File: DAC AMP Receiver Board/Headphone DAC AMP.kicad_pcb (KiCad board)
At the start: 4 copper layers, 55.2 x 67.7 mm, 75 parts, among them J3 SJ-3502-SMT, U1 ES9039Q2M, U2 TPS7A39, U3 TPA6120A2DWP, U4 OPA1612AxD, U5 OPA1612AxD, U6 TPS7A20xxxDQN

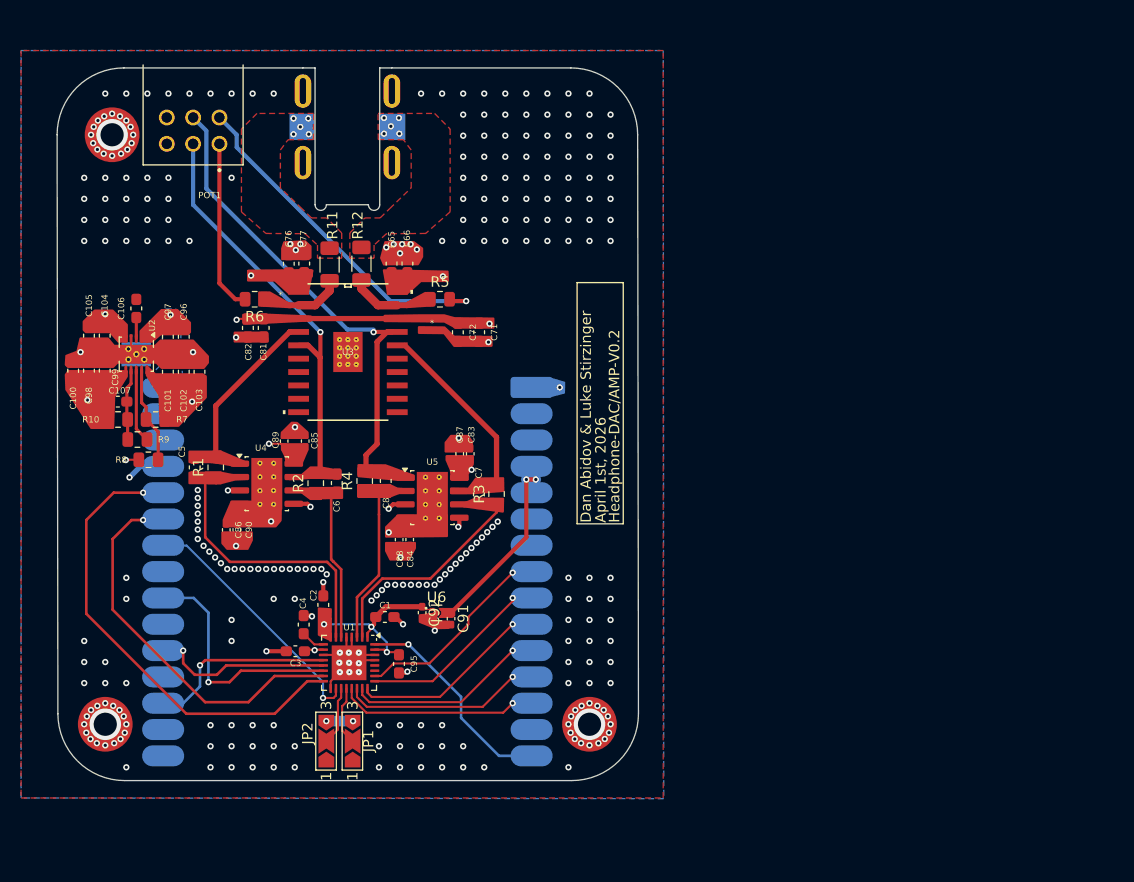
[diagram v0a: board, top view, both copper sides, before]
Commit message: Boards in same project, not panelized yet
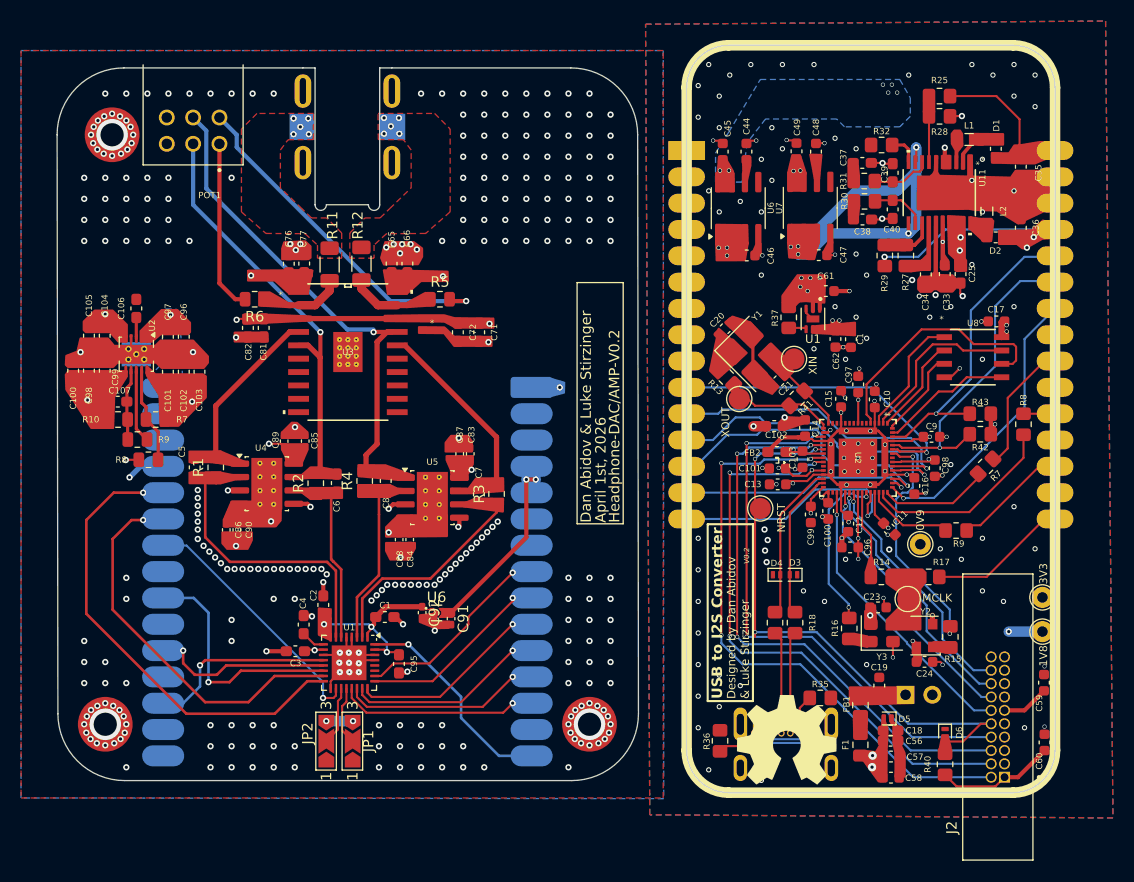
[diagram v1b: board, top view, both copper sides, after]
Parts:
- added 0V9: TestPoint_Probe, TestPoint:TestPoint_THTPad_D2.0mm_Drill1.0mm, F.Cu at (164.0, 98.3)
- added 1V8: TestPoint_Probe, TestPoint:TestPoint_THTPad_D2.0mm_Drill1.0mm, F.Cu at (175.6, 106.6)
- added 3V3: TestPoint_Probe, TestPoint:TestPoint_THTPad_D2.0mm_Drill1.0mm, F.Cu at (175.6, 103.3)
- added B**: Castellated Pins, Library:Castellated Hole PCB, F.Cu at (159.3, 60.9)
- added C1: 10u, Capacitor_SMD:C_0603_1608Metric, F.Cu at (157.4, 78.8)
- added C10: 100n, Capacitor_SMD:C_0603_1608Metric, F.Cu at (159.6, 84.5)
- added C100: 100n, Capacitor_SMD:C_0603_1608Metric, F.Cu at (155.2, 95.1)
- added C101: 100n, Capacitor_SMD:C_0603_1608Metric, F.Cu at (150.4, 91.1)
- added C102: 100n, Capacitor_SMD:C_0603_1608Metric, F.Cu at (150.1, 87.1)
- added C103: 1u, Capacitor_SMD:C_0603_1608Metric, F.Cu at (152.8, 90.2)
- added C11: 100n, Capacitor_SMD:C_0603_1608Metric, F.Cu at (161.0, 96.9)
- added C12: 100n, Capacitor_SMD:C_0603_1608Metric, F.Cu at (157.1, 96.3)
- added C13: 100n, Capacitor_SMD:C_0603_1608Metric, F.Cu at (150.4, 92.6)
- added C14: 100n, Capacitor_SMD:C_0603_1608Metric, F.Cu at (153.0, 87.3)
- added C15: 100n, Capacitor_SMD:C_0603_1608Metric, F.Cu at (156.4, 84.5)
- added C16: 100n, Capacitor_SMD:C_0603_1608Metric, F.Cu at (163.4, 92.8)
- added C17: 100n, Capacitor_SMD:C_0603_1608Metric, F.Cu at (171.2, 77.1)
- added C18: 100n, Capacitor_SMD:C_0603_1608Metric, F.Cu at (161.1, 116.0)
- added C19: 100n, Capacitor_SMD:C_0603_1608Metric, F.Cu at (160.1, 111.7)
- added C20: 18p, Capacitor_SMD:C_0603_1608Metric, F.Cu at (145.4, 77.8)
- added C21: 18p, Capacitor_SMD:C_0603_1608Metric, F.Cu at (150.5, 82.8)
- added C23: 100n, Capacitor_SMD:C_0603_1608Metric, F.Cu at (160.0, 104.3)
- added C24: 100n, Capacitor_SMD:C_0603_1608Metric, F.Cu at (164.4, 109.5)
- added C25: 10u, Capacitor_SMD:C_0603_1608Metric_Pad1.08x0.95mm_HandSolder, F.Cu at (167.8, 72.6)
- added C33: 1u, Capacitor_SMD:C_0603_1608Metric_Pad1.08x0.95mm_HandSolder, F.Cu at (166.3, 72.6)
- added C34: 1u, Capacitor_SMD:C_0603_1608Metric_Pad1.08x0.95mm_HandSolder, F.Cu at (164.5, 72.7)
- added C35: 10u, Capacitor_SMD:C_0603_1608Metric_Pad1.08x0.95mm_HandSolder, F.Cu at (173.5, 62.4)
- added C36: 10u, Capacitor_SMD:C_0603_1608Metric_Pad1.08x0.95mm_HandSolder, F.Cu at (173.5, 68.2)
- added C37: 330p, Capacitor_SMD:C_0603_1608Metric_Pad1.08x0.95mm_HandSolder, F.Cu at (158.5, 62.1)
- added C38: 18n, Capacitor_SMD:C_0603_1608Metric_Pad1.08x0.95mm_HandSolder, F.Cu at (158.5, 67.5)
- added C39: 22p, Capacitor_SMD:C_0603_1608Metric_Pad1.08x0.95mm_HandSolder, F.Cu at (161.3, 63.0)
- added C40: 39p, Capacitor_SMD:C_0603_1608Metric_Pad1.08x0.95mm_HandSolder, F.Cu at (161.3, 66.5)
- added C44: 1u, Capacitor_SMD:C_0603_1608Metric, F.Cu at (147.5, 61.0)
- added C45: 1u, Capacitor_SMD:C_0603_1608Metric, F.Cu at (145.2, 61.0)
- added C46: 10u, Capacitor_SMD:C_0603_1608Metric, F.Cu at (147.5, 70.9)
- added C47: 10u, Capacitor_SMD:C_0603_1608Metric, F.Cu at (154.3, 70.8)
- added C48: 1u, Capacitor_SMD:C_0603_1608Metric, F.Cu at (154.1, 61.0)
- added C49: 1u, Capacitor_SMD:C_0603_1608Metric, F.Cu at (152.2, 61.0)
- added C56: 100n, Capacitor_SMD:C_0603_1608Metric, F.Cu at (161.1, 117.0)
- added C57: 1u, Capacitor_SMD:C_0603_1608Metric, F.Cu at (161.2, 118.5)
- added C58: 1u, Capacitor_SMD:C_0603_1608Metric, F.Cu at (161.2, 120.5)
- added C59: 100n, Capacitor_SMD:C_0603_1608Metric, F.Cu at (175.7, 111.4)
- added C60: 100n, Capacitor_SMD:C_0603_1608Metric, F.Cu at (175.8, 117.1)
- added C61: 1u, Capacitor_SMD:C_0603_1608Metric, F.Cu at (155.0, 74.2)
- added C62: 10u, Capacitor_SMD:C_0603_1608Metric, F.Cu at (155.9, 78.8)
- added C9: 100n, Capacitor_SMD:C_0603_1608Metric, F.Cu at (165.0, 88.1)
- added C96: 100n, Capacitor_SMD:C_0603_1608Metric, F.Cu at (157.3, 98.6)
- added C97: 100n, Capacitor_SMD:C_0603_1608Metric, F.Cu at (158.1, 83.1)
- added C98: 100n, Capacitor_SMD:C_0603_1608Metric, F.Cu at (165.3, 91.1)
- added C99: 100n, Capacitor_SMD:C_0603_1608Metric, F.Cu at (153.6, 95.5)
- added D1: D_Schottky, Capacitor_SMD:C_0603_1608Metric_Pad1.08x0.95mm_HandSolder, F.Cu at (171.1, 60.7)
- added D2: D_Schottky, Capacitor_SMD:C_0603_1608Metric_Pad1.08x0.95mm_HandSolder, F.Cu at (171.1, 69.1)
- added D3: PESD5V0L1BSL, Diode_SMD:D_SOD-882, F.Cu at (151.9, 101.2)
- added D4: PESD5V0L1BSL, Diode_SMD:D_SOD-882, F.Cu at (150.3, 101.2)
- added D5: PESD5V0L1BSL, Diode_SMD:D_SOD-882, F.Cu at (160.9, 114.8)
- added D6: PESD5V0L1BSL, Diode_SMD:D_SOD-882, F.Cu at (166.3, 116.2)
- added F1: 2A, Fuse:Fuse_0805_2012Metric_Pad1.15x1.40mm_HandSolder, F.Cu at (158.3, 117.3)
- added FB1: 220R, Capacitor_SMD:C_0805_2012Metric_Pad1.18x1.45mm_HandSolder, F.Cu at (158.3, 113.6)
- added FB2: 600R @ 100MHz, Capacitor_SMD:C_0603_1608Metric_Pad1.08x0.95mm_HandSolder, F.Cu at (150.4, 89.5)
- added G***: LOGO, LOGO, F.Cu at (151.3, 116.9)
- added G***: LOGO, LOGO, B.Cu at (168.8, 120.9)
- added G***: LOGO, LOGO, B.Cu at (168.8, 80.9)
- added G***: LOGO, LOGO, B.Cu at (148.8, 120.9)
- added G***: LOGO, LOGO, B.Cu at (148.8, 100.9)
- added G***: LOGO, LOGO, B.Cu at (168.8, 100.9)
- added G***: LOGO, LOGO, B.Cu at (148.8, 80.9)
- added G***: LOGO, LOGO, B.Cu at (148.8, 60.9)
- added G***: LOGO, LOGO, B.Cu at (168.8, 60.9)
- added J1: 2137160001, 2137160001:MOLEX_2137160001, B.Cu at (151.2, 122.5)
- added J2: M50-3551042, M50_3551042:HARWIN_M50-3551042, F.Cu at (171.3, 114.7)
- added J4: PINHD_1x2_Male, Connector_PinHeader_2.54mm:PinHeader_1x02_P2.54mm_Vertical, B.Cu at (162.6, 112.6)
- added L1: 0.82u, Inductor_SMD:L_0805_2012Metric, F.Cu at (168.6, 59.9)
- added L2: 10u, Inductor_SMD:L_0805_2012Metric, F.Cu at (170.3, 66.7)
- added MCLK: TestPoint_Probe, TestPoint:TestPoint_Pad_D2.0mm, F.Cu at (162.8, 103.5)
- added NRST: TestPoint_Probe, TestPoint:TestPoint_Pad_D2.0mm, F.Cu at (148.8, 94.9)
- added R13: 220, Resistor_SMD:R_0805_2012Metric_Pad1.20x1.40mm_HandSolder, F.Cu at (145.5, 82.4)
- added R14: 22, Resistor_SMD:R_0805_2012Metric_Pad1.20x1.40mm_HandSolder, F.Cu at (160.3, 101.4)
- added R15: 22, Resistor_SMD:R_0805_2012Metric_Pad1.20x1.40mm_HandSolder, F.Cu at (166.8, 107.1)
- added R16: 22, Resistor_SMD:R_0805_2012Metric_Pad1.20x1.40mm_HandSolder, F.Cu at (157.2, 106.3)
- added R17: 22, Resistor_SMD:R_0805_2012Metric_Pad1.20x1.40mm_HandSolder, F.Cu at (164.8, 101.4)
- added R18: 22, Resistor_SMD:R_0805_2012Metric_Pad1.20x1.40mm_HandSolder, F.Cu at (152.1, 105.7)
- added R19: 22, Resistor_SMD:R_0805_2012Metric_Pad1.20x1.40mm_HandSolder, F.Cu at (150.2, 105.7)
- added R25: 13K, Resistor_SMD:R_0805_2012Metric_Pad1.20x1.40mm_HandSolder, F.Cu at (165.8, 57.6)
- added R27: 10.7k, Resistor_SMD:R_0805_2012Metric_Pad1.20x1.40mm_HandSolder, F.Cu at (162.6, 70.9)
- added R28: 84.5K, Resistor_SMD:R_0805_2012Metric_Pad1.20x1.40mm_HandSolder, F.Cu at (165.8, 55.7)
- added R29: 90.9k, Resistor_SMD:R_0805_2012Metric_Pad1.20x1.40mm_HandSolder, F.Cu at (160.6, 70.9)
- added R30: 9.09k, Resistor_SMD:R_0805_2012Metric_Pad1.20x1.40mm_HandSolder, F.Cu at (158.7, 65.7)
- added R31: 15k, Resistor_SMD:R_0805_2012Metric_Pad1.20x1.40mm_HandSolder, F.Cu at (158.6, 63.8)
- added R32: DNP, Resistor_SMD:R_0805_2012Metric_Pad1.20x1.40mm_HandSolder, F.Cu at (160.3, 60.4)
- added R35: 5.1k, Resistor_SMD:R_0805_2012Metric_Pad1.20x1.40mm_HandSolder, F.Cu at (154.5, 112.9)
- added R36: 5.1k, Resistor_SMD:R_0805_2012Metric_Pad1.20x1.40mm_HandSolder, F.Cu at (144.9, 117.0)
- added R37: 100k, Resistor_SMD:R_0805_2012Metric_Pad1.20x1.40mm_HandSolder, F.Cu at (151.5, 76.7)
- added R40: 10K, Resistor_SMD:R_0805_2012Metric_Pad1.20x1.40mm_HandSolder, F.Cu at (166.3, 119.2)
- added R41: 1M, Resistor_SMD:R_0805_2012Metric_Pad1.20x1.40mm_HandSolder, F.Cu at (152.3, 84.4)
- added R42: 2k, Resistor_SMD:R_0805_2012Metric_Pad1.20x1.40mm_HandSolder, F.Cu at (169.7, 87.8)
- added R43: 2k, Resistor_SMD:R_0805_2012Metric_Pad1.20x1.40mm_HandSolder, F.Cu at (169.7, 85.9)
- added R7: 10, Resistor_SMD:R_0805_2012Metric_Pad1.20x1.40mm_HandSolder, F.Cu at (170.2, 90.9)
- added R8: 10, Resistor_SMD:R_0805_2012Metric_Pad1.20x1.40mm_HandSolder, F.Cu at (173.8, 86.9)
- added R9: 10, Resistor_SMD:R_0805_2012Metric_Pad1.20x1.40mm_HandSolder, F.Cu at (167.4, 97.0)
- added U1: NCV8187AMTW090TAG, NCV8187AMTW090TAG:SON65P200X200X80-7N, F.Cu at (153.8, 76.9)
- added U11: ADP5071AREZ-R7, ADP5071:RE-20-1_ADI, F.Cu at (165.8, 64.9)
- added U2: XU316-1024-QF60B-C24, footprints:QFN_F60B-C24_XMO, F.Cu at (158.0, 90.1)
- added U6: MCP1727-1802xSN, Package_SO:SOIC-8_3.9x4.9mm_P1.27mm, F.Cu at (146.7, 66.4)
- added U7: MCP1727-3302xSN, Package_SO:SOIC-8_3.9x4.9mm_P1.27mm, F.Cu at (153.5, 66.3)
- added U8: W25Q16JVSNIQ, W25Q16JVSNIQ:SOIC_150MIL_WIN, F.Cu at (169.0, 80.5)
- added XIN: TestPoint_Probe, TestPoint:TestPoint_Pad_D2.0mm, F.Cu at (152.0, 80.7)
- added XOUT: TestPoint_Probe, TestPoint:TestPoint_Pad_D2.0mm, F.Cu at (146.8, 84.5)
- added Y1: Crystal_GND24, Crystal:Crystal_SMD_3225-4Pin_3.2x2.5mm_HandSoldering, F.Cu at (148.0, 80.2)
- added Y2: LMK6CE049152CDLFR, Oscillator:Oscillator_SMD_EuroQuartz_XO32-4Pin_3.2x2.5mm, F.Cu at (164.4, 107.0)
- added Y3: ASDLJ-E-45.1584MHz, Oscillator:Oscillator_SMD_Abracon_ASE-4Pin_3.2x2.5mm, F.Cu at (160.3, 106.7)
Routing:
- net +3.3V: track 0.00 -> 187.2 mm, vias 0 -> 17
- net +1V8: track 0.00 -> 63.4 mm, vias 0 -> 13
- net /Debug/TMS: track 0.00 -> 58.0 mm, vias 0 -> 3
- net /Debug/TCK: track 0.00 -> 55.1 mm, vias 0 -> 3
- net /Debug/XMOS_NRST: track 0.00 -> 55.1 mm, vias 0 -> 3
- net /Debug/TDO: track 0.00 -> 54.5 mm, vias 0 -> 3
- net /Debug/TDI: track 0.00 -> 53.3 mm, vias 0 -> 3
- net 0V9: track 0.00 -> 48.0 mm, vias 0 -> 18
- net GND: track 32.3 -> 74.9 mm, vias 294 -> 411
- net /General Power/5Vin: track 0.00 -> 39.4 mm, vias 0 -> 10
- net /I2C_SCL: track 0.00 -> 30.3 mm, vias 0 -> 1
- net /GPIO4: track 0.00 -> 29.9 mm, vias 0 -> 1
- net /I2C_SDA: track 0.00 -> 29.6 mm, vias 0 -> 1
- net /GPIO5: track 0.00 -> 29.3 mm, vias 0 -> 1
- net /GPIO6: track 0.00 -> 29.3 mm, vias 0 -> 1
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- added copper zone on B.Cu, net +1V8
- added copper zone on In2.Cu, net +1V8
- added copper zone on In2.Cu, net +3.3V
- added copper zone on In2.Cu, net /General Power/5Vin
- added copper zone on In2.Cu, net /USB Audio Input/VBUS
- added copper zone on In2.Cu, net 0V9
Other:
- board size 55.2 x 67.7 mm -> 94.8 x 71 mm
- board text added: "Designed by Dan Abidov & Luke Stirzinger"
- board text added: "USB to I2S Converter"
- board text added: "V0.2"
